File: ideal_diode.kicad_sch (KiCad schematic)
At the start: 8 parts, among them Q901 BC857BS, Q902 AO3401A, Q903 BC857BS, Q904 AO3401A

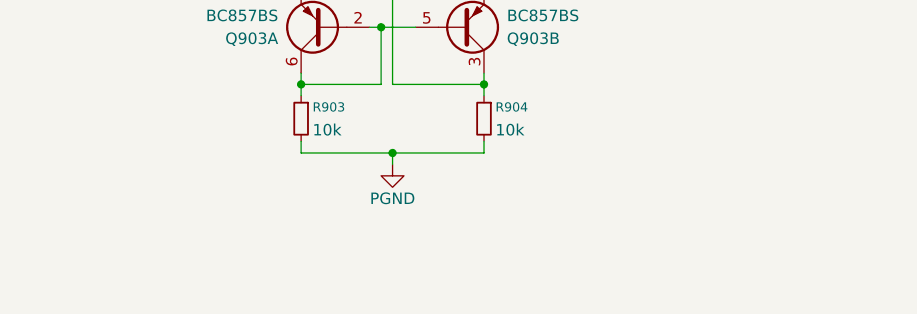
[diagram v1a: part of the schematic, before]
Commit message: added sim link into ideal diode
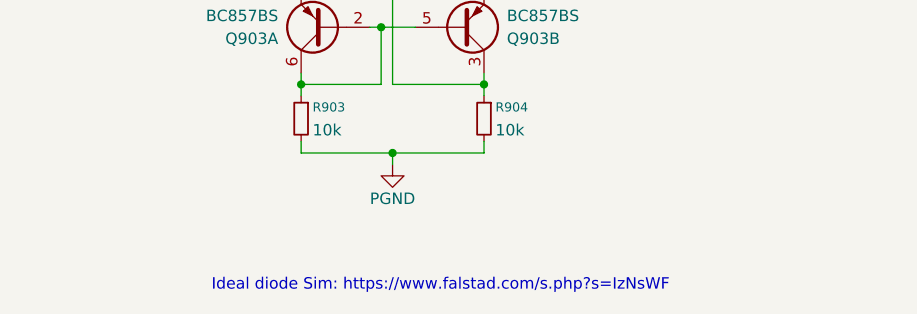
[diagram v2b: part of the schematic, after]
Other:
- note added: "Ideal diode Sim: https://www.falstad.com/s.php?s=IzNsWF"
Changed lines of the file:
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@@
 	(generator_version "10.0")
 	(paper "A4")
+	(text "Ideal diode Sim: https://www.falstad.com/s.php?s=IzNsWF"
+		(exclude_from_sim no)
+		(at 85.344 140.462 0)
+		(effects
+			(font
+				(size 1.27 1.27)
+			)
+		)
+	)
 	(junction
 		(at 69.85 55.88)
